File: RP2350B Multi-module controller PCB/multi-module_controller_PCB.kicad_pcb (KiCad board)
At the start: 4 copper layers, 59.8 x 84.4 mm, 85 parts, among them J1 Conn_02x06_Odd_Even, J10 Internal unused GPIO Breakout, J4 SM03B-SRSS-TB, J5 USB_C_Receptacle_USB2.0_14P, J6 USB_C_Receptacle_USB2.0_14P, J7 Module_Bay, J8 USB_A, J9 ADC_Breakout, SW1 SW_Push, SW10 BTN_MDL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

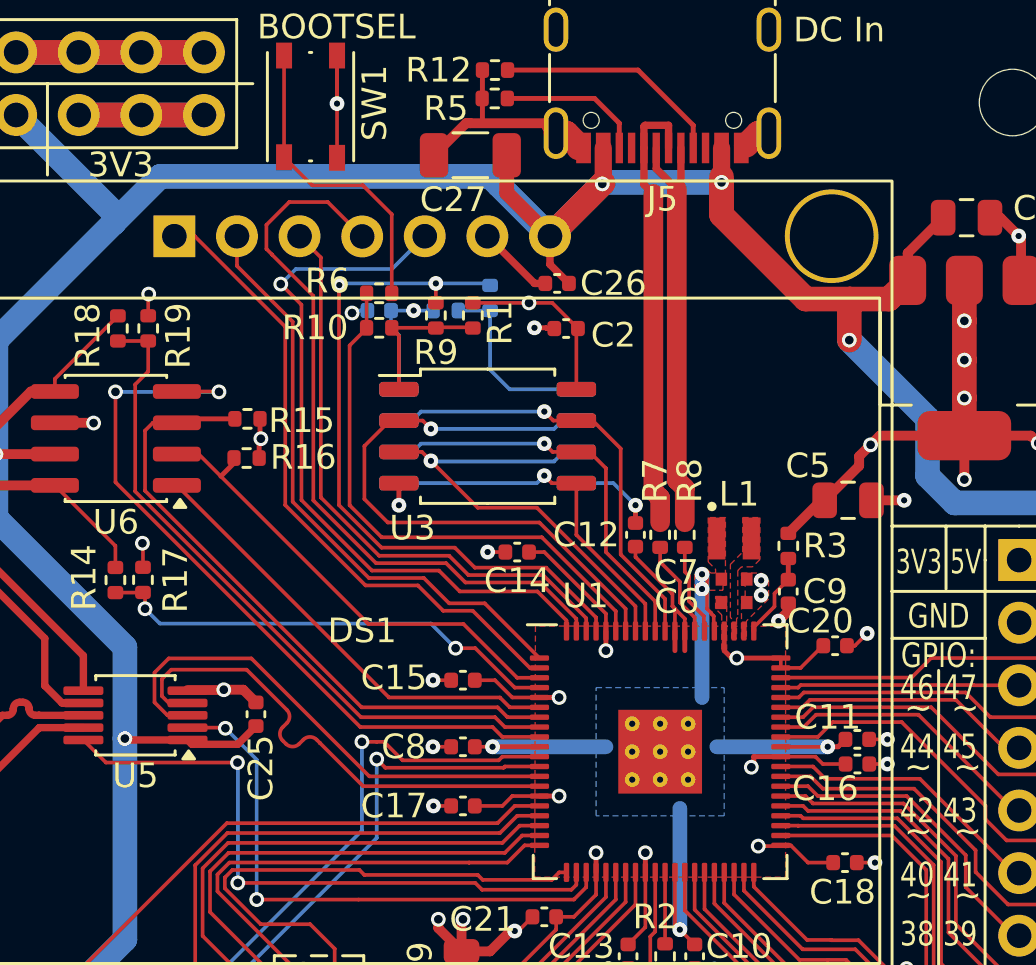
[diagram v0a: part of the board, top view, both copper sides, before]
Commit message: update PCB to drive OLED from 3v3 rail
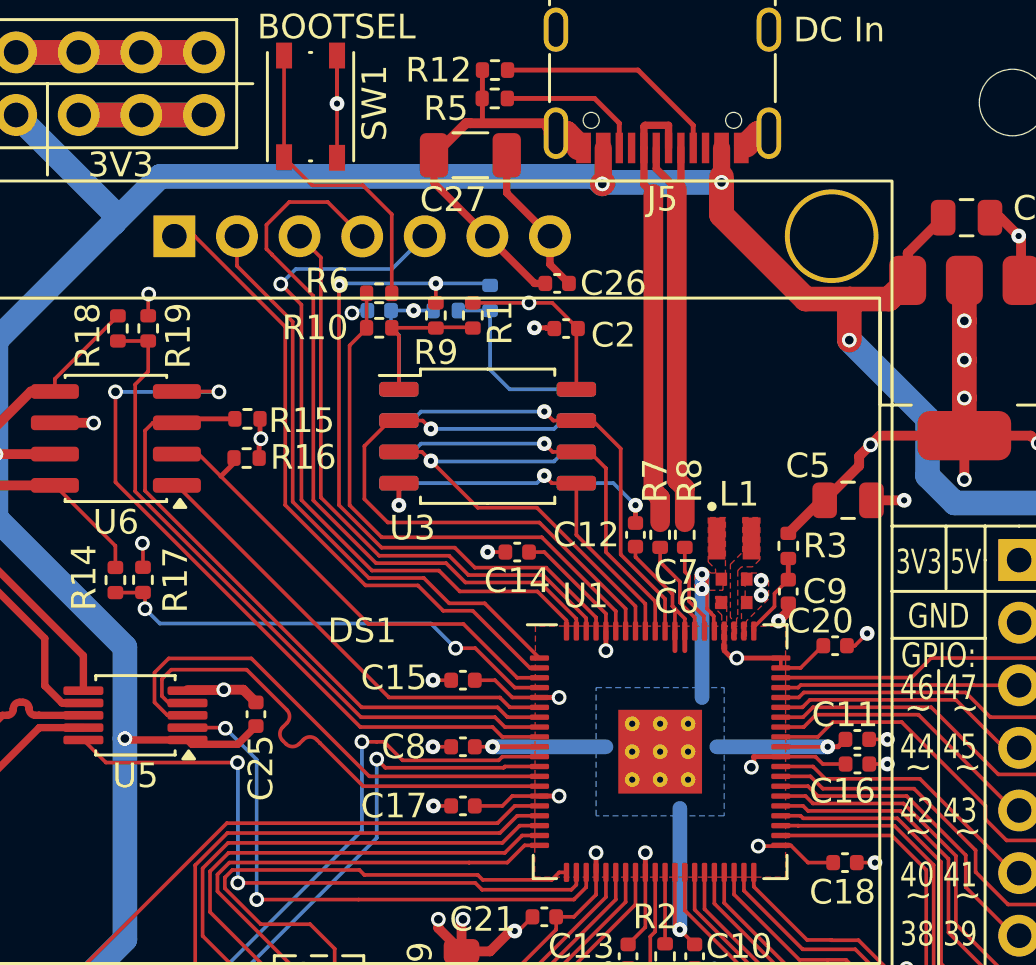
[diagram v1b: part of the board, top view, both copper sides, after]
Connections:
- C26 pad 1: VBUS -> +3V3
- C27 pad 1: VBUS -> +3V3
- DS1 pad 7: VBUS -> +3V3
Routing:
- net VBUS: track 171.9 -> 160.8 mm
- net +3V3: track 94.3 -> 100.6 mm
- net GND: track 156.0 -> 160.1 mm
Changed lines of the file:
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@@
 		(sheetname "/")
 		(sheetfile "multi-module_controller_PCB.kicad_sch")
+		(units
+			(unit
+				(name "A")
+				(pins "1" "2")
+			)
+		)
 		(attr smd)
 		(duplicate_pad_numbers_are_jumpers no)
@@
 			)
 		)
+		(property "LCSC" "C1525"
+			(at 0 0 180)
+			(unlocked yes)
+			(layer "F.Fab")
+			(hide yes)
+			(effects
+				(font
+					(size 1 1)
+					(thickness 0.15)
+				)
+			)
+		)
 		(property ki_fp_filters "C_*")
 		(sheetname "/")
 		(sheetfile "multi-module_controller_PCB.kicad_sch")
+		(units
+			(unit
+				(name "A")
+				(pins "1" "2")
+			)
+		)
 		(attr smd)
 		(duplicate_pad_numbers_are_jumpers no)
@@
 		(tags "capacitor")
 		(property "Reference" "C16"
-			(at -1.305 1 0)
+			(at -0.605 1.1 0)
 			(layer "F.SilkS")
 			(effects
@@
 		(sheetname "/")
 		(sheetfile "multi-module_controller_PCB.kicad_sch")
+		(units
+			(unit
+				(name "A")
+				(pins "1" "2")
+			)
+		)
 		(attr smd)
 		(duplicate_pad_numbers_are_jumpers no)
@@
 		(sheetname "/")
 		(sheetfile "multi-module_controller_PCB.kicad_sch")
+		(units
+			(unit
+				(name "A")
+				(pins "1" "2")
+			)
+		)
 		(attr smd)
 		(duplicate_pad_numbers_are_jumpers no)
@@
 		(sheetname "/")
 		(sheetfile "multi-module_controller_PCB.kicad_sch")
+		(units
+			(unit
+				(name "A")
+				(pins "1" "2" "3" "4" "5" "7" "6")
+			)
+		)
 		(attr through_hole)
 		(duplicate_pad_numbers_are_jumpers no)
@@
 			(layers "*.Cu" "*.Mask")
 			(remove_unused_layers no)
-			(net "VBUS")
+			(net "+3V3")
 			(pinfunction "VCC_7")
 			(pintype "power_in")
@@
 			)
 		)
-		(property "LCSC" ""
+		(property "LCSC" "C16780"
 			(at 0 0 270)
 			(unlocked yes)
@@
 			(layers "F.Cu" "F.Mask" "F.Paste")
 			(roundrect_rratio 0.25)
-			(net "VBUS")
+			(net "+3V3")
 			(pintype "passive")
 		)
@@
 			(layers "F.Cu" "F.Mask" "F.Paste")
 			(roundrect_rratio 0.217391)
-			(net "VBUS")
+			(net "+3V3")
 			(pintype "passive")
 		)
@@
 		(tags "capacitor")
 		(property "Reference" "C11"
-			(at -1.2 -0.9 0)
+			(at -0.5 -1 0)
 			(layer "F.SilkS")
 			(effects
@@
 	)
 	(segment
+		(start 95.53 79.0842)
+		(end 93.775 77.3292)
+		(width 0.3)
+		(layer "F.Cu")
+		(net "+3V3")
+	)
+	(segment
 		(start 108.075 88.4)
 		(end 106.675 89.8)
@@
 	)
 	(segment
+		(start 93.775 77.3292)
+		(end 93.775 75.8)
+		(width 0.3)
+		(layer "F.Cu")
+		(net "+3V3")
+	)
+	(segment
 		(start 102.6 95.9)
 		(end 102.9 96.2)
@@
 	)
 	(segment
+		(start 95.53 80.23)
+		(end 96.3 81)
+		(width 0.3)
+		(layer "F.Cu")
+		(net "+3V3")
+	)
+	(segment
 		(start 92.48 102.2)
 		(end 93.6 102.2)
@@
 	)
 	(segment
+		(start 95.53 79.0842)
+		(end 95.53 80.23)
+		(width 0.3)
+		(layer "F.Cu")
+		(net "+3V3")
+	)
+	(segment
 		(start 99.4 104.61)
 		(end 99.4 107.12)
@@
 	)
 	(segment
+		(start 90.825 76.9192)
+		(end 90.825 75.8)
+		(width 0.3)
+		(layer "F.Cu")
+		(net "GND")
+	)
+	(segment
 		(start 64.8464 91.3566)
 		(end 64.8464 90.8366)
@@
 	)
 	(segment
+		(start 92.99 79.0842)
+		(end 90.825 76.9192)
+		(width 0.3)
+		(layer "F.Cu")
+		(net "GND")
+	)
+	(segment
 		(start 94.1 107.2755)
 		(end 93.9245 107.2755)
@@
 	)
 	(segment
-		(start 93.775 77.3292)
-		(end 93.775 75.8)
-		(width 0.6)
-		(layer "F.Cu")
-		(net "VBUS")
-	)
-	(segment
 		(start 80.8233 99.524)
 		(end 80.998299 99.698999)
@@
 	)
 	(segment
-		(start 95.53 80.23)
-		(end 96.3 81)
-		(width 0.3)
-		(layer "F.Cu")
-		(net "VBUS")
-	)
-	(segment
 		(start 102.4922 76.9)
 		(end 102.4922 76.6746)
@@
 	)
 	(segment
-		(start 95.53 79.0842)
-		(end 95.53 80.23)
-		(width 0.3)
-		(layer "F.Cu")
-		(net "VBUS")
-	)
-	(segment
-		(start 97.0771 77.5371)
-		(end 97.6521 76.9621)
-		(width 1)
-		(layer "F.Cu")
-		(net "VBUS")
-	)
-	(segment
 		(start 64.4162 138.5034)
 		(end 65.3436 137.576)
@@
 	)
 	(segment
-		(start 95.53 79.0842)
-		(end 97.0771 77.5371)
-		(width 1)
-		(layer "F.Cu")
-		(net "VBUS")
-	)
-	(segment
 		(start 73.87 74.165)
 		(end 68.79 74.165)
@@
 	)
 	(segment
-		(start 95.53 79.0842)
-		(end 93.775 77.3292)
-		(width 0.6)
-		(layer "F.Cu")
-		(net "VBUS")
-	)
-	(segment
 		(start 78.3404 99.524)
 		(end 78.2828 99.4664)
@@
 	)
 	(segment
-		(start 93.4586 77.0128)
-		(end 93.103 76.6572)
-		(width 1)
-		(layer "B.Cu")
-		(net "VBUS")
-	)
-	(segment
-		(start 97.6521 76.9621)
-		(end 95.53 79.0842)
-		(width 1)
-		(layer "B.Cu")
-		(net "VBUS")
-	)
-	(segment
 		(start 77.8361 78.5361)
 		(end 73.0504 83.3218)
@@
 	)
 	(segment
-		(start 93.103 76.6572)
-		(end 79.715 76.6572)
-		(width 1)
-		(layer "B.Cu")
-		(net "VBUS")
-	)
-	(segment
 		(start 73.0504 83.3218)
 		(end 73.0504 87.9348)
@@
 	)
 	(segment
-		(start 97.7142 76.9)
-		(end 97.6521 76.9621)
-		(width 1)
-		(layer "B.Cu")
-		(net "VBUS")
-	)
-	(segment
 		(start 62.8932 123.0068)
 		(end 62.8932 129.4004)
@@
 	)
 	(segment
-		(start 95.53 79.0842)
-		(end 93.4586 77.0128)
-		(width 1)
-		(layer "B.Cu")
-		(net "VBUS")
-	)
-	(segment
 		(start 62.8834 135.9966)
 		(end 60.7 138.18)
@@
 	)
 	(segment
+		(start 79.715 76.6572)
+		(end 77.8361 78.5361)
+		(width 1)
+		(layer "B.Cu")
+		(net "VBUS")
+	)
+	(segment
 		(start 115.789681 89.9076)
 		(end 116.905 91.022919)
@@
 	)
 	(segment
-		(start 79.715 76.6572)
-		(end 77.8361 78.5361)
+		(start 97.6521 76.9621)
+		(end 97.3472 76.6572)
+		(width 1)
+		(layer "B.Cu")
+		(net "VBUS")
+	)
+	(segment
+		(start 97.3472 76.6572)
+		(end 79.715 76.6572)
 		(width 1)
 		(layer "B.Cu")

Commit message: Update PCB files for v1.1
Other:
- board text added: "1.1"
- board text added: "V1.1 2025-2026"
- board text removed: "1.0"
- board text removed: "V1.0 2025-2026"
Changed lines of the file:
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@@
 		)
 	)
-	(gr_text "1.0"
+	(gr_text "1.1"
 		(at 92.8 150.8 0)
 		(layer "F.SilkS")
@@
 		)
 	)
-	(gr_text "V1.0      2025-2026"
+	(gr_text "V1.1      2025-2026"
 		(at 89.1 152.7 0)
 		(layer "B.SilkS")

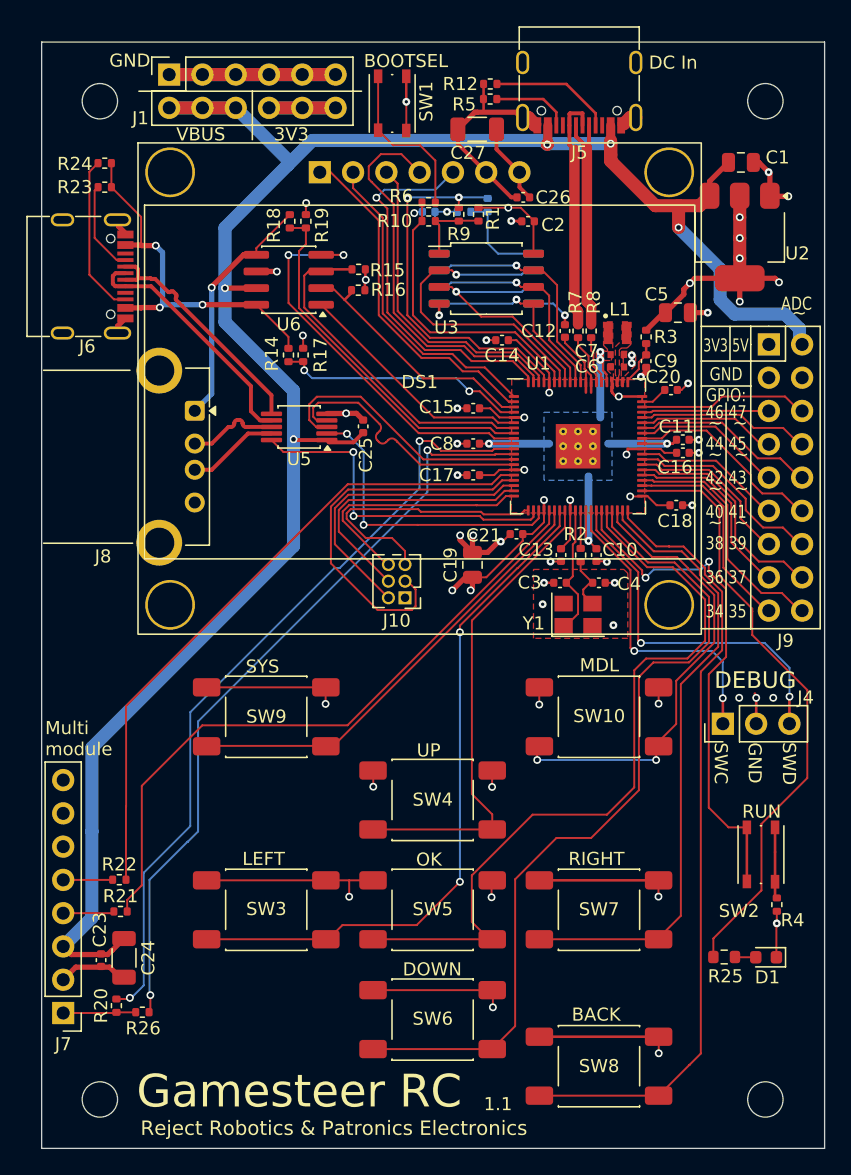
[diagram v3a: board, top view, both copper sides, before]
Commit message: Add SD Card slot to underside of board, wired for use with SPI1. Reconfigure button pinout and use J10 pins for this purpose
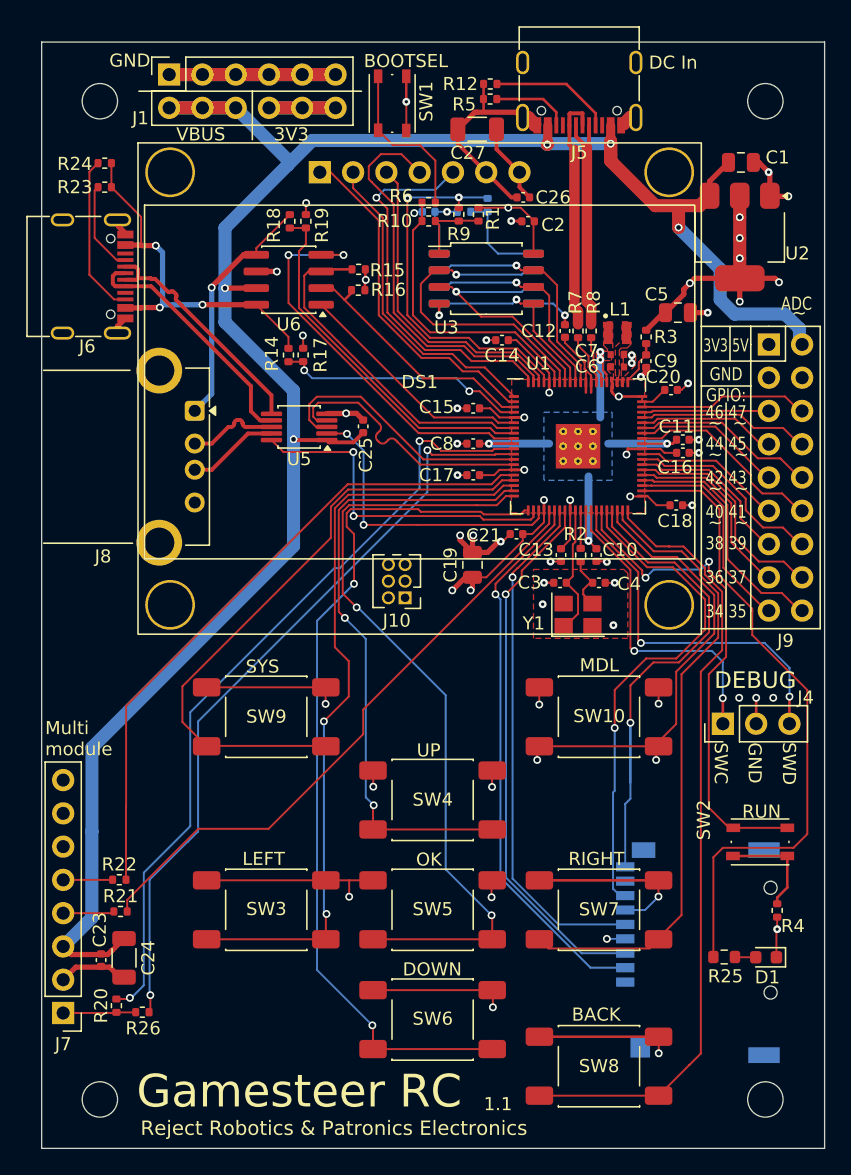
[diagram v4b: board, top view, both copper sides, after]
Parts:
- added J11: Micro_SD_Card_Det1, EasyEDA:SD-SMD_MLD-TF-PUSH-H18, B.Cu at (108.9, 138.7)
- moved SW2 0.97 mm to (113.9, 130.2), turned to 180 degrees
- moved R4 0.44 mm to (115.2, 135.4)
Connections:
- J10 pad 2: /GPIO18 -> unconnected-(J10-Pin_2-Pad2)
- J10 pad 3: /GPIO17 -> unconnected-(J10-Pin_3-Pad3)
- J10 pad 4: /GPIO19 -> unconnected-(J10-Pin_4-Pad4)
- J10 pad 5: /GPIO21 -> unconnected-(J10-Pin_5-Pad5)
- J10 pad 6: /GPIO20 -> unconnected-(J10-Pin_6-Pad6)
- SW3 pad 2: /GPIO26 -> /GPIO18
- SW4 pad 2: /GPIO27 -> /GPIO19
- SW5 pad 2: /GPIO28 -> /GPIO20
- SW6 pad 2: /GPIO29 -> /GPIO21
- SW9 pad 2: /GPIO25 -> /GPIO17
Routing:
- net /GPIO21: track 21.2 -> 67.5 mm, vias 0 -> 2
- net /GPIO20: track 19.1 -> 60.1 mm, vias 0 -> 2
- net /GPIO18: track 22.9 -> 57.7 mm, vias 0 -> 2
- net /GPIO19: track 21.0 -> 48.7 mm, vias 0 -> 2
- net /GPIO29: track 64.5 -> 39.9 mm, vias 0 -> 1
- net /GPIO28: track 59.4 -> 38.5 mm, vias 0 -> 1
- net /GPIO17: track 29.5 -> 48.3 mm
- net /GPIO26: track 52.9 -> 39.7 mm, vias 2 -> 1
- net /GPIO25: track 34.7 -> 42.4 mm, vias 0 -> 1
- net /GPIO27: track 37.0 -> 41.4 mm, vias 0 -> 1
- net /GPIO24: track 50.4 -> 47.1 mm
- net /GPIO33: track 46.4 -> 49.6 mm
- net Net-(R4-Pad1): track 5.44 -> 8.31 mm
- net GND: track 160.1 -> 162.7 mm
- net +3V3: track 100.6 -> 102.0 mm, vias 19 -> 20
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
